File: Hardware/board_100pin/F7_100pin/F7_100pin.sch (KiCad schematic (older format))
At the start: 81 parts, among them IC1 OPA659IDBVR, IC2 OPA659IDBVR, IC3 LMH6643MAX_NOPB, IC4 LT1935ES5, J1 SMA Edge, J2 Pre-Amp, J3 UART, J4 5V, J5 Filter, J6 3V3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

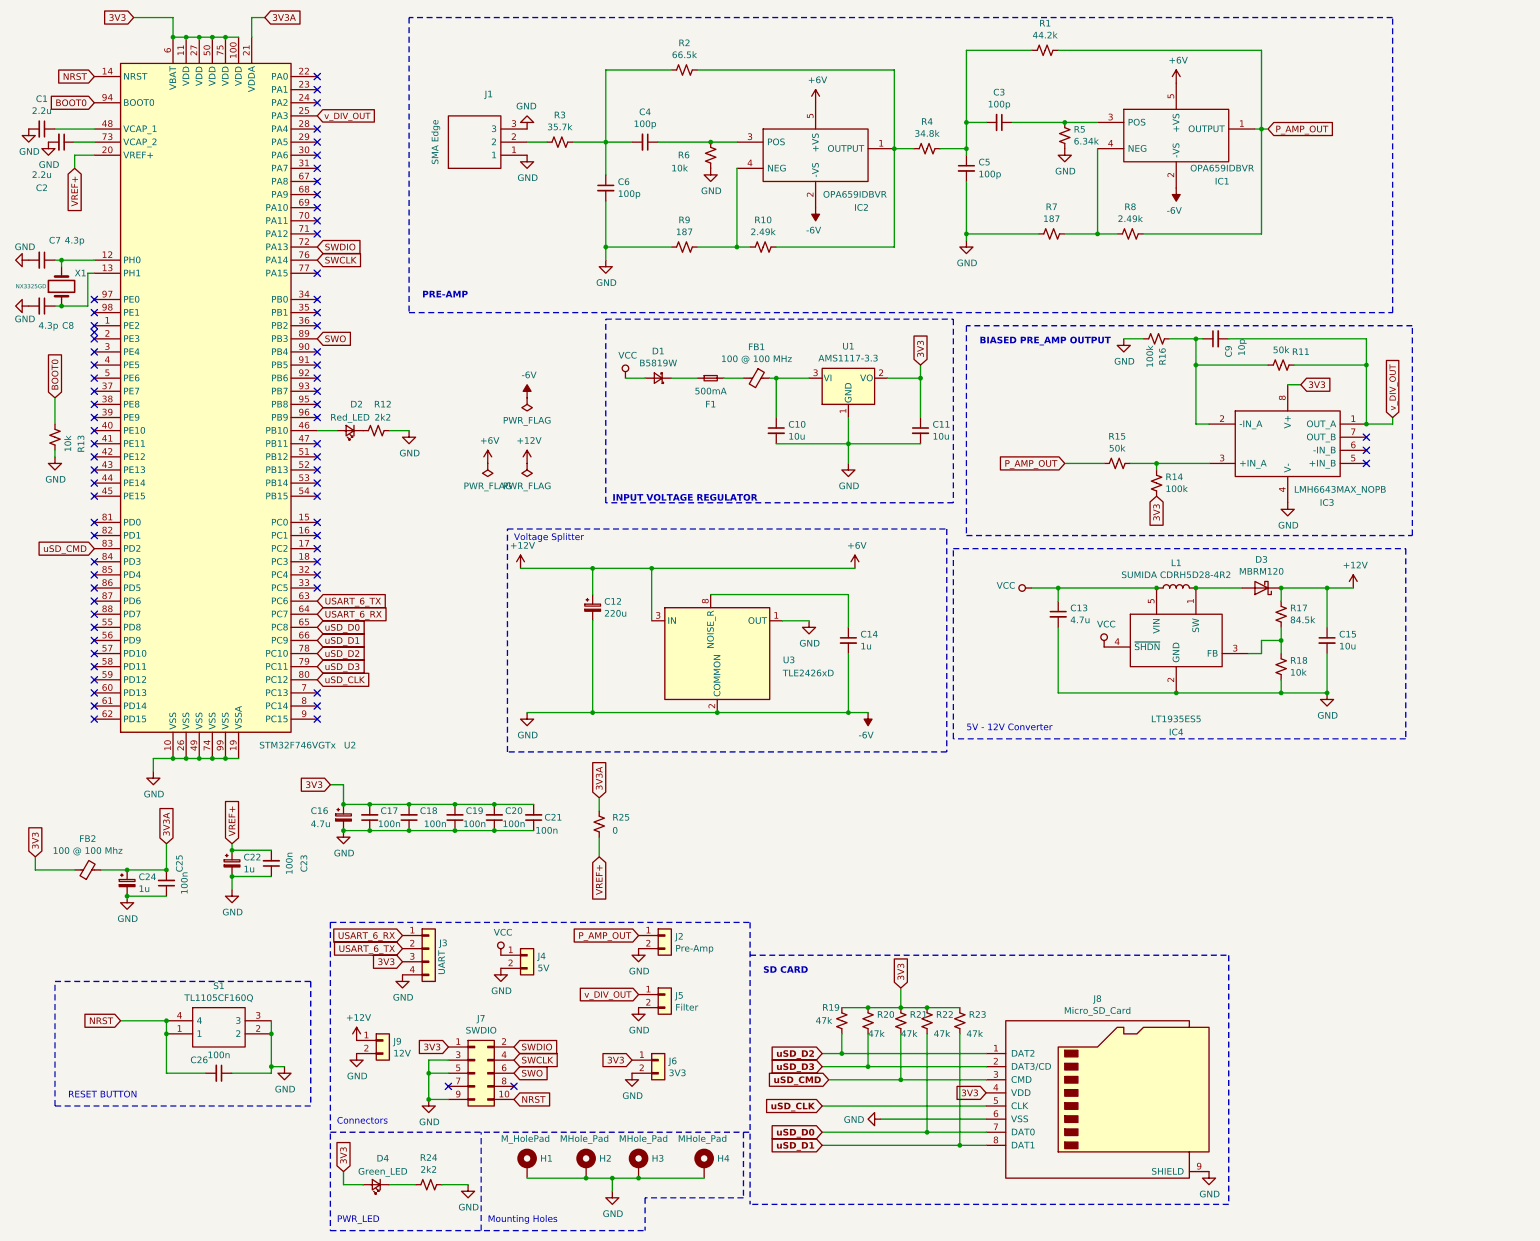
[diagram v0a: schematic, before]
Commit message: Added 100 pin version
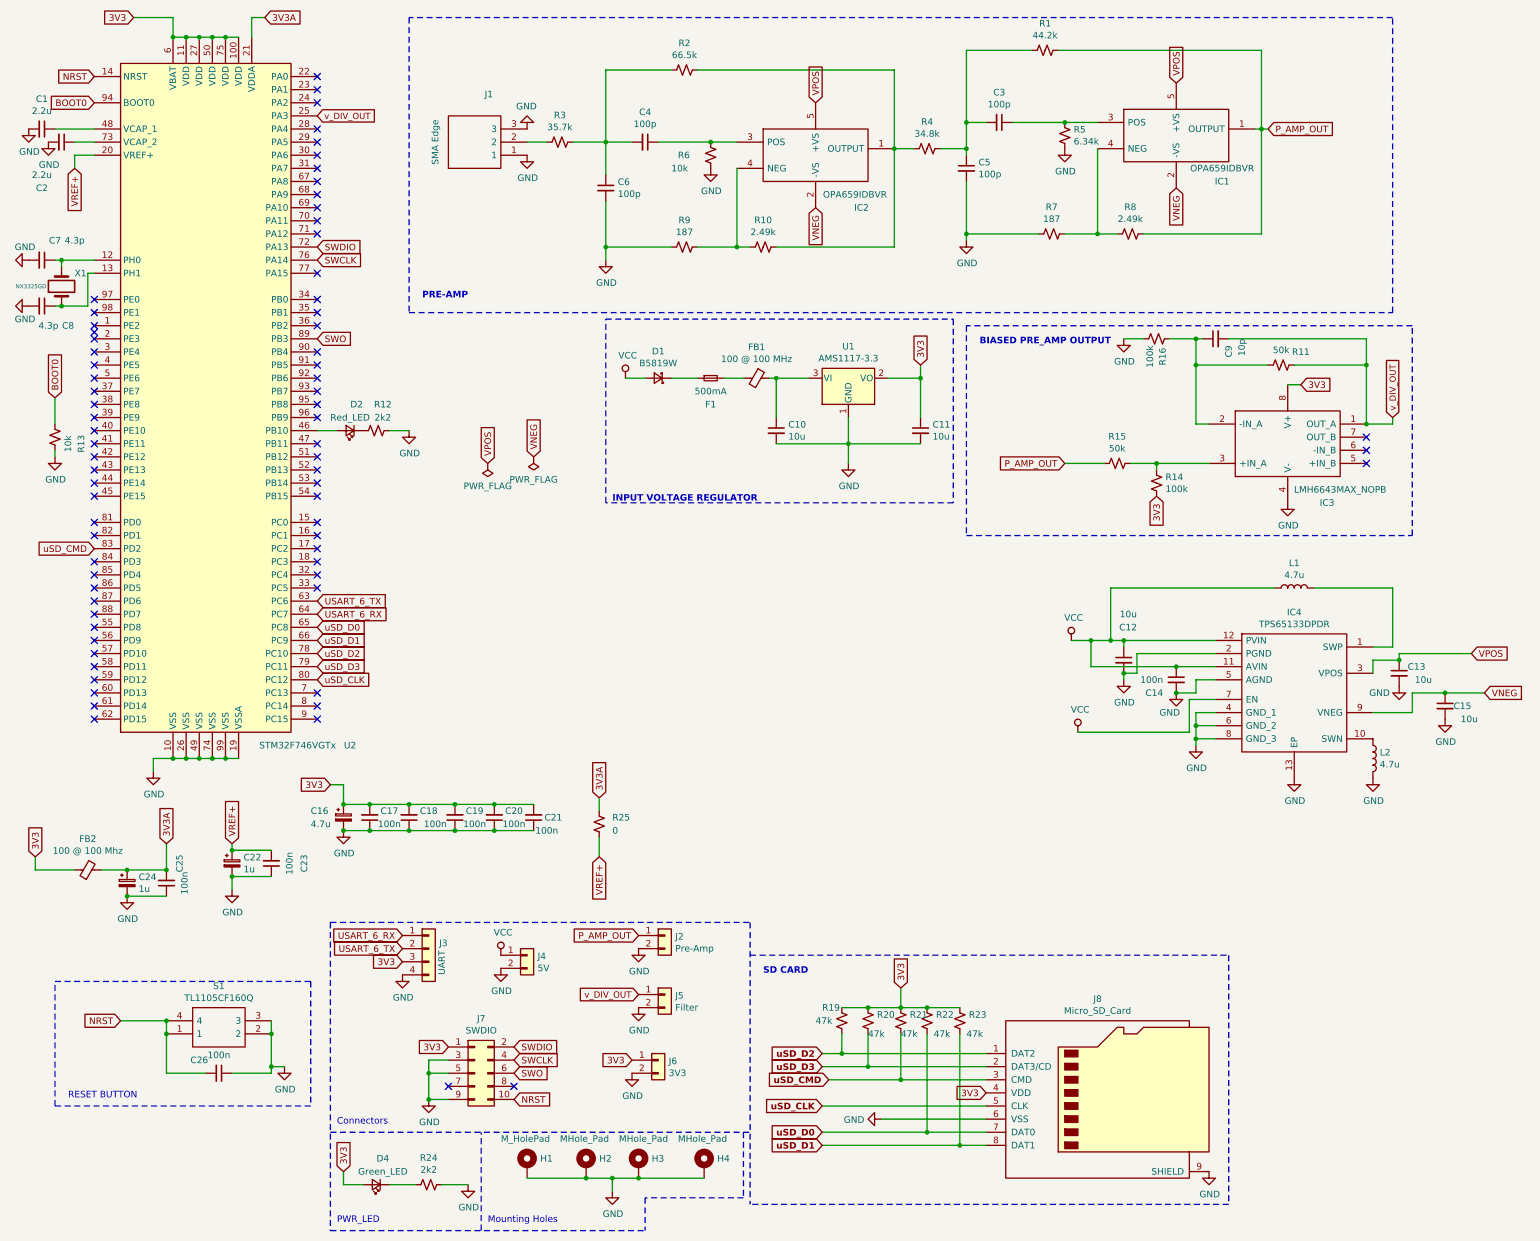
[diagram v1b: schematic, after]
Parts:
- removed C12: 220u, Capacitor_Tantalum_SMD:CP_EIA-3216-18_Kemet-A, symbol Device:CP_Small
- removed D3: MBRM120, Diode_SMD:D_Powermite_AK, symbol Device:D_Schottky
- removed IC4: LT1935ES5, SamacSys_Parts:SOT95P280X100-5N, symbol SamacSys_Parts:LT1935ES5
- removed J9: 12V, Connector_PinHeader_2.54mm:PinHeader_1x02_P2.54mm_Vertical, symbol Connector_Generic:Conn_01x02
- removed R17: 84.5k, Resistor_SMD:R_0603_1608Metric, symbol Device:R_Small_US
- removed R18: 10k, Resistor_SMD:R_0603_1608Metric, symbol Device:R_Small_US
- removed U3: TLE2426xD, Package_SO:SOIC-8_3.9x4.9mm_P1.27mm, symbol Reference_Voltage:TLE2426xD
- added C12: 10u, Capacitor_SMD:C_0805_2012Metric, symbol Device:C_Small
- added IC4: TPS65133DPDR, SamacSys_Parts:SON45P300X300X80-13N-D, symbol SamacSys_Parts:TPS65133DPDR
- added L2: 4.7u, Inductor_SMD:L_Coilcraft_XxL4020, symbol Device:L
- C13: value 4.7u -> 10u; footprint Capacitor_SMD:C_0603_1608Metric -> Capacitor_SMD:C_0805_2012Metric
- C14: value 1u -> 100n; footprint Capacitor_SMD:C_0603_1608Metric -> Capacitor_SMD:C_0805_2012Metric
- C15: footprint Capacitor_SMD:C_0603_1608Metric -> Capacitor_SMD:C_0805_2012Metric
- L1: value SUMIDA CDRH5D28-4R2 -> 4.7u; footprint SamacSys_Parts:INDPM5757X300N -> Inductor_SMD:L_Coilcraft_XxL4020
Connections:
- net VCC: now also C14.1, C12.1, IC4.11 (AVIN), IC4.12 (PVIN), IC4.7 (EN); no longer C13.1
- net at L1.2: now also IC4.1 (SWP)
- net +12V renamed VPOS
- net VPOS: now also C13.1, IC4.3 (VPOS); no longer C15.1
- net -6V renamed GND
- net GND: now also C12.2, IC4.13 (EP), IC4.2 (PGND), IC4.4 (GND_1), IC4.5 (AGND), IC4.6 (GND_2), IC4.8 (GND_3), L2.2; no longer IC1.2 (-VS), IC2.2 (-VS)
- new net: IC4.10 (SWN), L2.1
- new net VNEG: C15.1, IC1.2 (-VS), IC2.2 (-VS), IC4.9 (VNEG)
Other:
- note removed: "5V - 12V Converter"
- note removed: "Voltage Splitter\n"

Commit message: Updated F7 100 pin schematic
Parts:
- S1: symbol SamacSys_Parts:TL1105CF160Q -> SamacSys_Parts:TL1105CF160Q_0
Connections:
- net GND: now also S1.4; no longer S1.2
- net NRST: now also S1.2; no longer S1.4
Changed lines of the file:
@@
 Text Notes 4100 9800 0    50   ~ 0
 Mounting Holes\n
-$Comp
-L SamacSys_Parts:TL1105CF160Q S1
-U 1 1 5F163850
-P 1650 8250
-F 0 "S1" H 2050 8515 50  0000 C CNN
-F 1 "TL1105CF160Q" H 2050 8424 50  0000 C CNN
-F 2 "SamacSys_Parts:TL1105CF160Q" H 2300 8350 50  0001 L CNN
-F 3 "https://componentsearchengine.com/Datasheets/1/TL1105CF160Q.pdf" H 2300 8250 50  0001 L CNN
-F 4 "Tactile Switches 6X6X8MM 160GF" H 2300 8150 50  0001 L CNN "Description"
-F 5 "8" H 2300 8050 50  0001 L CNN "Height"
-F 6 "E-Switch" H 2300 7950 50  0001 L CNN "Manufacturer_Name"
-F 7 "TL1105CF160Q" H 2300 7850 50  0001 L CNN "Manufacturer_Part_Number"
-F 8 "612-TL1105C" H 2300 7750 50  0001 L CNN "Mouser Part Number"
-F 9 "https://www.mouser.com/Search/Refine.aspx?Keyword=612-TL1105C" H 2300 7650 50  0001 L CNN "Mouser Price/Stock"
-	1    1650 8250
-	1    0    0    -1
-$EndComp
-$Comp
-L Device:C_Small C26
-U 1 1 5F16641C
-P 2050 8650
-F 0 "C26" V 1950 8500 50  0000 C CNN
-F 1 "100n" V 1912 8650 50  0000 C CNN
-F 2 "Capacitor_SMD:C_0402_1005Metric" H 2050 8650 50  0001 C CNN
-F 3 "~" H 2050 8650 50  0001 C CNN
-	1    2050 8650
-	0    1    1    0
-$EndComp
-Wire Wire Line
-	2150 8650 2450 8650
-Wire Wire Line
-	2450 8650 2450 8600
-Connection ~ 2450 8350
-Wire Wire Line
-	2450 8350 2450 8250
-Wire Wire Line
-	1950 8650 1650 8650
-Wire Wire Line
-	1650 8650 1650 8350
-Connection ~ 1650 8350
-Wire Wire Line
-	1650 8350 1650 8250
-$Comp
-L power:GND #PWR032
-U 1 1 5F1716CA
-P 2550 8600
-F 0 "#PWR032" H 2550 8350 50  0001 C CNN
-F 1 "GND" H 2555 8427 50  0000 C CNN
-F 2 "" H 2550 8600 50  0001 C CNN
-F 3 "" H 2550 8600 50  0001 C CNN
-	1    2550 8600
-	1    0    0    -1
-$EndComp
-Wire Wire Line
-	2550 8600 2450 8600
-Connection ~ 2450 8600
-Wire Wire Line
-	2450 8600 2450 8350
-Text GLabel 1300 8250 0    50   Input ~ 0
-NRST
-Wire Wire Line
-	1650 8250 1300 8250
-Connection ~ 1650 8250
 Wire Notes Line
 	2750 7950 2750 8900
@@
 Wire Notes Line
 	800  8900 800  7950
-Wire Notes Line
-	800  7950 2750 7950
 Text Notes 900  8850 0    50   ~ 0
 RESET BUTTON\n
@@
 	9050 5600 8950 5600
 Connection ~ 8950 5600
+Wire Notes Line
+	800  7950 2750 7950
+Wire Wire Line
+	2550 8600 2450 8600
+Connection ~ 2450 8600
+Wire Wire Line
+	2450 8650 2450 8600
+Wire Wire Line
+	2150 8650 2450 8650
+Wire Wire Line
+	1650 8250 1300 8250
+Wire Wire Line
+	1950 8650 1650 8650
+Connection ~ 1650 8250
+Connection ~ 1650 8350
+Wire Wire Line
+	1650 8350 1650 8250
+Wire Wire Line
+	1650 8650 1650 8350
+Wire Wire Line
+	2450 8600 2450 8350
+Wire Wire Line
+	2450 8350 2450 8250
+Connection ~ 2450 8350
+$Comp
+L SamacSys_Parts:TL1105CF160Q_0 S1
+U 1 1 5F163850
+P 1650 8250
+F 0 "S1" H 2050 8515 50  0000 C CNN
+F 1 "TL1105CF160Q" H 2050 8424 50  0000 C CNN
+F 2 "SamacSys_Parts:TL1105CF160Q" H 2300 8350 50  0001 L CNN
+F 3 "https://componentsearchengine.com/Datasheets/1/TL1105CF160Q.pdf" H 2300 8250 50  0001 L CNN
+F 4 "Tactile Switches 6X6X8MM 160GF" H 2300 8150 50  0001 L CNN "Description"
+F 5 "8" H 2300 8050 50  0001 L CNN "Height"
+F 6 "E-Switch" H 2300 7950 50  0001 L CNN "Manufacturer_Name"
+F 7 "TL1105CF160Q" H 2300 7850 50  0001 L CNN "Manufacturer_Part_Number"
+F 8 "612-TL1105C" H 2300 7750 50  0001 L CNN "Mouser Part Number"
+F 9 "https://www.mouser.com/Search/Refine.aspx?Keyword=612-TL1105C" H 2300 7650 50  0001 L CNN "Mouser Price/Stock"
+	1    1650 8250
+	1    0    0    -1
+$EndComp
+$Comp
+L power:GND #PWR032
+U 1 1 5F1716CA
+P 2550 8600
+F 0 "#PWR032" H 2550 8350 50  0001 C CNN
+F 1 "GND" H 2555 8427 50  0000 C CNN
+F 2 "" H 2550 8600 50  0001 C CNN
+F 3 "" H 2550 8600 50  0001 C CNN
+	1    2550 8600
+	1    0    0    -1
+$EndComp
+$Comp
+L Device:C_Small C26
+U 1 1 5F16641C
+P 2050 8650
+F 0 "C26" V 1950 8500 50  0000 C CNN
+F 1 "100n" V 1912 8650 50  0000 C CNN
+F 2 "Capacitor_SMD:C_0402_1005Metric" H 2050 8650 50  0001 C CNN
+F 3 "~" H 2050 8650 50  0001 C CNN
+	1    2050 8650
+	0    1    1    0
+$EndComp
+Text GLabel 1300 8250 0    50   Input ~ 0
+NRST
 $EndSCHEMATC

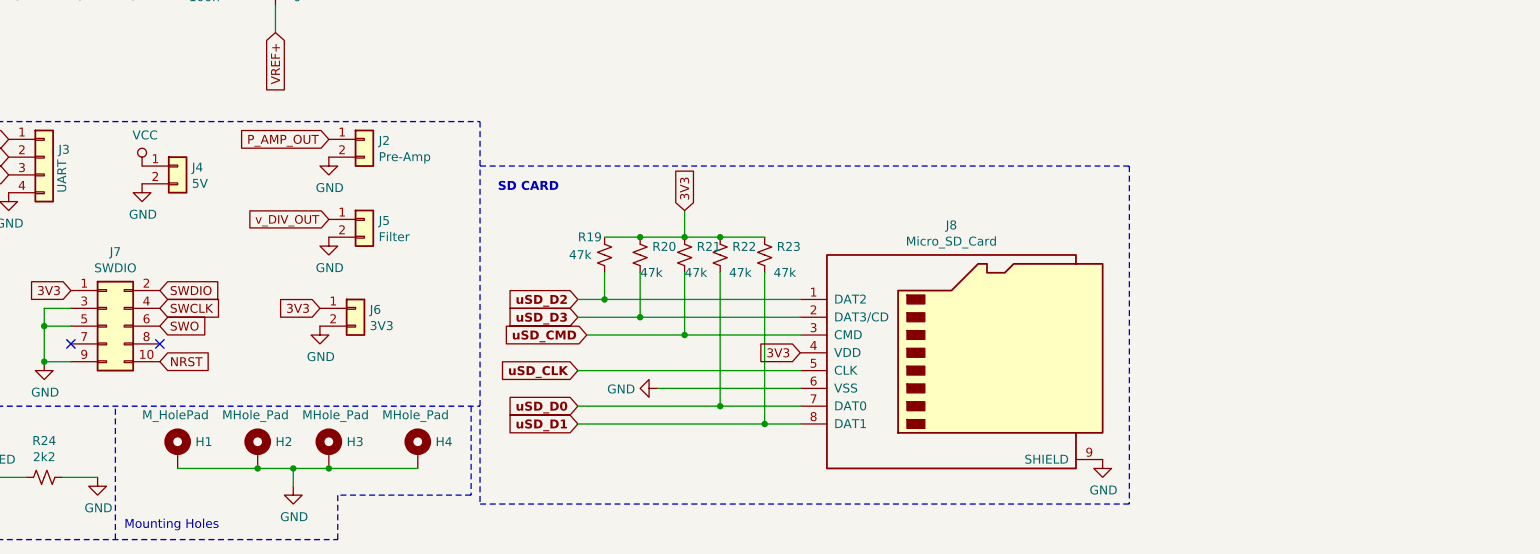
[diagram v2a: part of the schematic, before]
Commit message: Edited board to add USB power
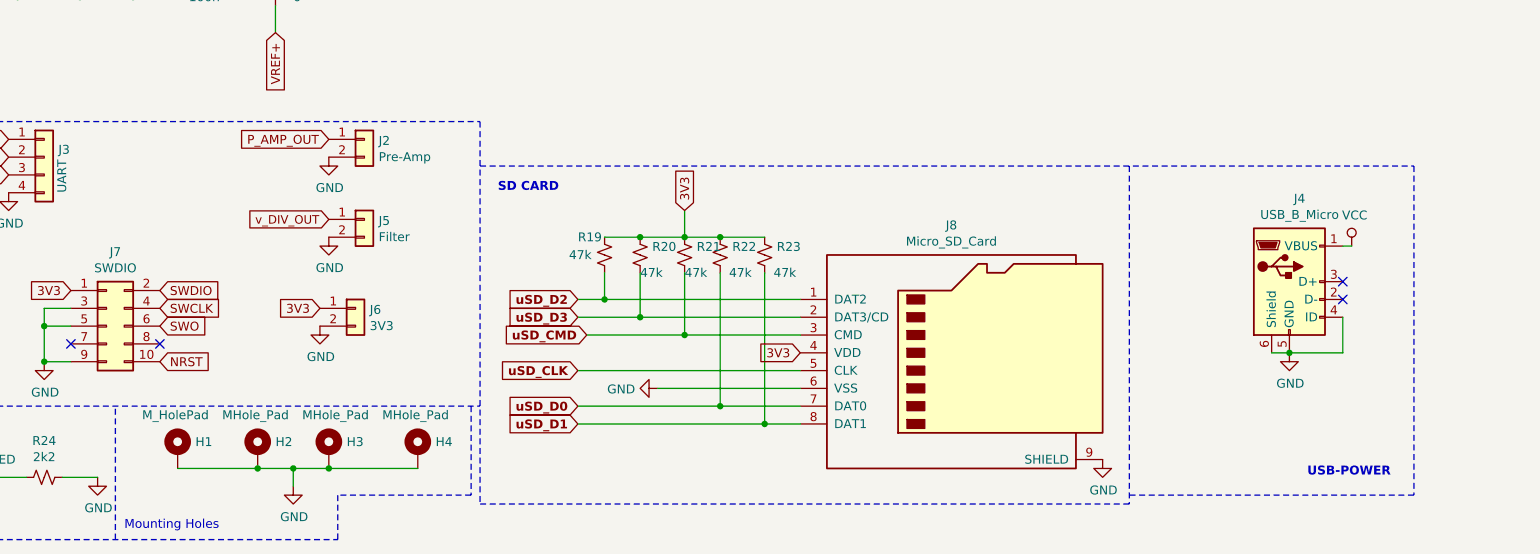
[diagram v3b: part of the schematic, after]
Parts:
- removed J4: 5V, Connector_PinHeader_2.54mm:PinHeader_1x02_P2.54mm_Vertical, symbol Connector_Generic:Conn_01x02
- added J4: USB_B_Micro, Connector_USB:USB_Micro-B_GCT_USB3076-30-A, symbol Connector:USB_B_Micro
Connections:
- net GND: now also J4.4 (ID), J4.5 (GND), J4.6 (Shield)
- net VCC: now also J4.1 (VBUS)
- no-connect marks 73 -> 75
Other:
- note added: "USB-POWER"
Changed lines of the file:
@@
 Wire Notes Line
 	9750 9650 6100 9650
-Wire Notes Line
-	6100 7750 9750 7750
 Text Notes 6200 7900 0    50   ~ 10
 SD CARD\n
@@
 $EndComp
 $Comp
-L Connector_Generic:Conn_01x02 J4
-U 1 1 5F0DC1B0
-P 4400 7750
-F 0 "J4" H 4480 7742 50  0000 L CNN
-F 1 "5V" H 4480 7651 50  0000 L CNN
-F 2 "Connector_PinHeader_2.54mm:PinHeader_1x02_P2.54mm_Vertical" H 4400 7750 50  0001 C CNN
-F 3 "~" H 4400 7750 50  0001 C CNN
-	1    4400 7750
-	1    0    0    -1
-$EndComp
-$Comp
 L Connector_Generic:Conn_01x04 J3
 U 1 1 5F0E43B6
@@
 F 3 "~" H 4000 8650 50  0001 C CNN
 	1    4000 8650
-	1    0    0    -1
-$EndComp
-$Comp
-L power:GND #PWR029
-U 1 1 5F0EA4B8
-P 4200 7850
-F 0 "#PWR029" H 4200 7600 50  0001 C CNN
-F 1 "GND" H 4205 7677 50  0000 C CNN
-F 2 "" H 4200 7850 50  0001 C CNN
-F 3 "" H 4200 7850 50  0001 C CNN
-	1    4200 7850
-	1    0    0    -1
-$EndComp
-$Comp
-L power:VCC #PWR028
-U 1 1 5F0EAE16
-P 4200 7750
-F 0 "#PWR028" H 4200 7600 50  0001 C CNN
-F 1 "VCC" H 4217 7923 50  0000 C CNN
-F 2 "" H 4200 7750 50  0001 C CNN
-F 3 "" H 4200 7750 50  0001 C CNN
-	1    4200 7750
 	1    0    0    -1
 $EndComp
@@
 Text GLabel 1300 8250 0    50   Input ~ 0
 NRST
+$Comp
+L Connector:USB_B_Micro J4
+U 1 1 5F5F74D2
+P 10650 8400
+F 0 "J4" H 10707 8867 50  0000 C CNN
+F 1 "USB_B_Micro" H 10707 8776 50  0000 C CNN
+F 2 "Connector_USB:USB_Micro-B_GCT_USB3076-30-A" H 10800 8350 50  0001 C CNN
+F 3 "~" H 10800 8350 50  0001 C CNN
+	1    10650 8400
+	1    0    0    -1
+$EndComp
+NoConn ~ 10950 8400
+NoConn ~ 10950 8500
+Wire Wire Line
+	10550 8800 10650 8800
+Wire Wire Line
+	10950 8600 10950 8800
+Wire Wire Line
+	10950 8800 10650 8800
+Connection ~ 10650 8800
+$Comp
+L power:VCC #PWR0101
+U 1 1 5F62C175
+P 11000 8200
+F 0 "#PWR0101" H 11000 8050 50  0001 C CNN
+F 1 "VCC" H 11017 8373 50  0000 C CNN
+F 2 "" H 11000 8200 50  0001 C CNN
+F 3 "" H 11000 8200 50  0001 C CNN
+	1    11000 8200
+	1    0    0    -1
+$EndComp
+Wire Wire Line
+	10950 8200 11000 8200
+$Comp
+L power:GND #PWR0102
+U 1 1 5F63A29E
+P 10650 8800
+F 0 "#PWR0102" H 10650 8550 50  0001 C CNN
+F 1 "GND" H 10655 8627 50  0000 C CNN
+F 2 "" H 10650 8800 50  0001 C CNN
+F 3 "" H 10650 8800 50  0001 C CNN
+	1    10650 8800
+	1    0    0    -1
+$EndComp
+Wire Notes Line
+	11350 7750 11350 9600
+Wire Notes Line
+	11350 9600 9750 9600
+Wire Notes Line
+	6100 7750 11350 7750
+Text Notes 10750 9500 0    50   ~ 10
+USB-POWER
 $EndSCHEMATC

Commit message: Added initial H7 Design
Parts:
- C16, C22, C24: symbol Device:CP_Small -> F7_100pin-rescue:CP_Small-Device
- FB1, FB2: symbol Device:Ferrite_Bead_Small -> F7_100pin-rescue:Ferrite_Bead_Small-Device
- J4: symbol Connector:USB_B_Micro -> F7_100pin-rescue:USB_B_Micro-Connector
